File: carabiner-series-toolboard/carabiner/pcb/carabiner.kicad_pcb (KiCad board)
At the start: 2 copper layers, 32.1 x 35.5 mm, 25 parts, among them J1 MF-Vertical 43045-1612, J2 MF-Horizontal 43045-1621, J7 MF-Horizontal 43045-1600

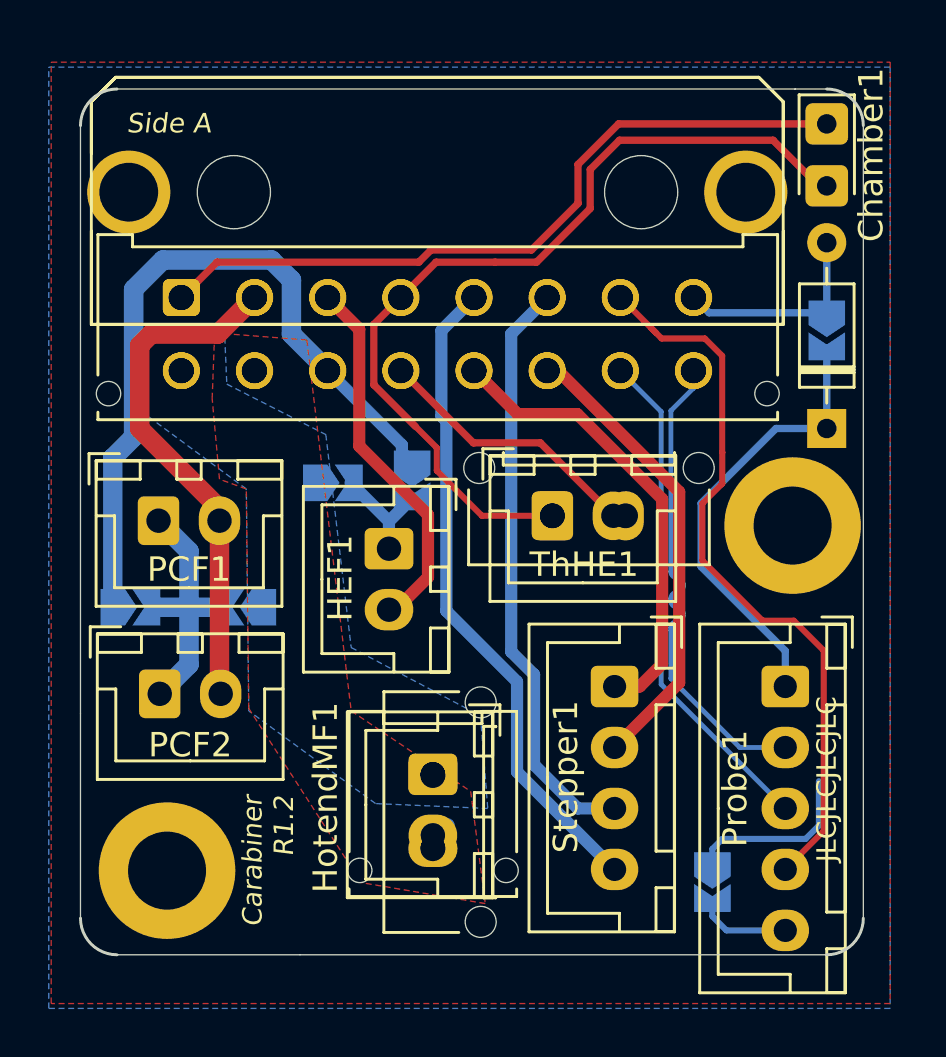
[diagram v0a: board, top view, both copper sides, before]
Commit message: Carabiner R1.2.1 - Fix all the things
- Fix disconnected A3 port (the 5th pin that duplicated A3 was disconnected)
- Match data lines closer - now within 0.04mm in length!
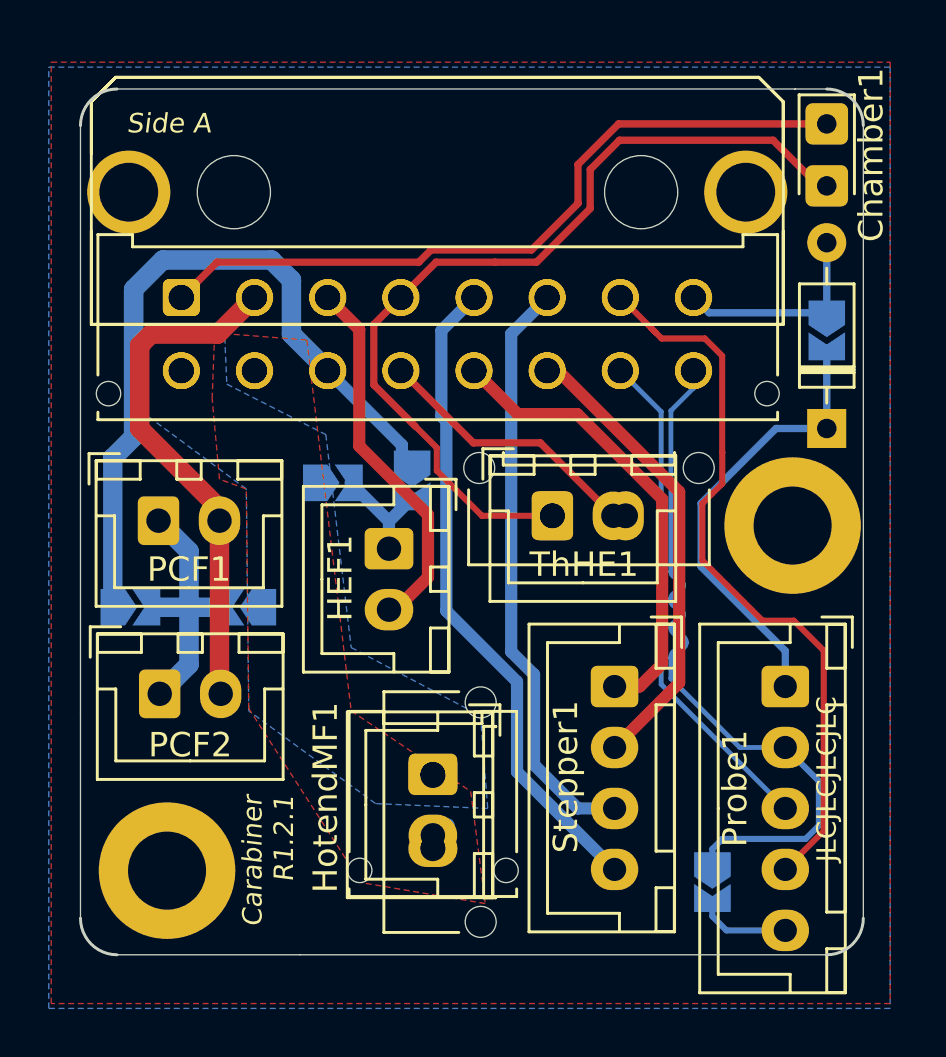
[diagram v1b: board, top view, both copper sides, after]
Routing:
- net A2+: track 27.5 -> 30.2 mm
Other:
- board text added: "Carabiner R1.2.1"
- board text removed: "Carabiner R1.2"
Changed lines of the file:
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@@
     (effects (font (size 0.7 0.7) (thickness 0.1)) (justify left mirror))
   )
-  (gr_text "Carabiner\nR1.2" (at 58.24 69.09 90) (layer "B.SilkS")
+  (gr_text "Carabiner\nR1.2.1" (at 58.24 69.09 90) (layer "B.SilkS")
     (effects (font (size 0.8 0.8) (thickness 0.15) italic) (justify right mirror))
   )
@@
     (effects (font (size 0.8 0.8) (thickness 0.15)))
   )
-  (gr_text "Carabiner\nR1.2" (at 58.2 62.97 90) (layer "F.SilkS")
+  (gr_text "Carabiner\nR1.2.1\n" (at 58.2 62.97 90) (layer "F.SilkS")
     (effects (font (size 0.8 0.8) (thickness 0.15) italic) (justify right))
   )
@@
   (segment (start 74.33 44.23) (end 73.915 43.815) (width 0.25) (layer "F.Cu") (net 10))
   (segment (start 76.1 44.23) (end 74.33 44.23) (width 0.25) (layer "F.Cu") (net 10))
-  (segment (start 75.63 46.27) (end 74.71 47.19) (width 0.2) (layer "B.Cu") (net 11))
+  (segment (start 74.71 54.89) (end 74.71 54.99) (width 0.2) (layer "B.Cu") (net 11))
+  (segment (start 75.039593 56.99) (end 75.01 56.99) (width 0.2) (layer "B.Cu") (net 11))
   (segment (start 76.82 64.75) (end 80.23 64.75) (width 0.25) (layer "B.Cu") (net 11))
   (segment (start 80.78 64.2) (end 80.78 62.38) (width 0.25) (layer "B.Cu") (net 11))
-  (segment (start 74.71 56.09) (end 74.71 56.19) (width 0.2) (layer "B.Cu") (net 11))
+  (segment (start 75.63 45.55) (end 75.63 46.27) (width 0.2) (layer "B.Cu") (net 11))
+  (segment (start 75.01 56.39) (end 75.039593 56.39) (width 0.2) (layer "B.Cu") (net 11))
+  (segment (start 77.536397 61) (end 79.4 61) (width 0.2) (layer "B.Cu") (net 11))
   (segment (start 74.71 47.19) (end 74.71 53.79) (width 0.2) (layer "B.Cu") (net 11))
+  (segment (start 75.21 55.49) (end 75.21 55.59) (width 0.2) (layer "B.Cu") (net 11))
   (segment (start 79.4 61) (end 79.4 60.63819) (width 0.25) (layer "B.Cu") (net 11))
-  (segment (start 74.71 54.89) (end 74.71 54.99) (width 0.2) (layer "B.Cu") (net 11))
   (segment (start 80.23 64.75) (end 80.78 64.2) (width 0.25) (layer "B.Cu") (net 11))
-  (segment (start 75.63 45.55) (end 75.63 46.27) (width 0.2) (layer "B.Cu") (net 11))
-  (segment (start 75.21 55.49) (end 75.21 55.59) (width 0.2) (layer "B.Cu") (net 11))
-  (segment (start 74.71 56.19) (end 74.71 58.173603) (width 0.2) (layer "B.Cu") (net 11))
+  (segment (start 74.71 57.29) (end 74.71 57.34) (width 0.2) (layer "B.Cu") (net 11))
+  (segment (start 75.63 46.27) (end 74.71 47.19) (width 0.2) (layer "B.Cu") (net 11))
   (segment (start 76.41 65.795) (end 76.41 65.16) (width 0.25) (layer "B.Cu") (net 11))
-  (segment (start 77.536397 61) (end 79.4 61) (width 0.2) (layer "B.Cu") (net 11))
+  (segment (start 75.21 54.29) (end 75.21 54.39) (width 0.2) (layer "B.Cu") (net 11))
+  (segment (start 80.78 62.38) (end 79.4 61) (width 0.25) (layer "B.Cu") (net 11))
   (segment (start 74.71 58.173603) (end 77.536397 61) (width 0.2) (layer "B.Cu") (net 11))
-  (segment (start 75.21 54.29) (end 75.21 54.39) (width 0.2) (layer "B.Cu") (net 11))
+  (segment (start 74.71 57.34) (end 74.71 58.173603) (width 0.2) (layer "B.Cu") (net 11))
   (segment (start 76.41 65.16) (end 76.82 64.75) (width 0.25) (layer "B.Cu") (net 11))
+  (arc (start 74.96 55.24) (mid 75.136777 55.313223) (end 75.21 55.49) (width 0.2) (layer "B.Cu") (net 11))
+  (arc (start 74.96 54.64) (mid 74.783223 54.713223) (end 74.71 54.89) (width 0.2) (layer "B.Cu") (net 11))
+  (arc (start 74.71 56.09) (mid 74.797868 56.302132) (end 75.01 56.39) (width 0.2) (layer "B.Cu") (net 11))
+  (arc (start 75.01 56.99) (mid 74.797868 57.077868) (end 74.71 57.29) (width 0.2) (layer "B.Cu") (net 11))
+  (arc (start 74.71 53.79) (mid 74.783223 53.966777) (end 74.96 54.04) (width 0.2) (layer "B.Cu") (net 11))
+  (arc (start 74.71 54.99) (mid 74.783223 55.166777) (end 74.96 55.24) (width 0.2) (layer "B.Cu") (net 11))
+  (arc (start 74.96 54.04) (mid 75.136777 54.113223) (end 75.21 54.29) (width 0.2) (layer "B.Cu") (net 11))
+  (arc (start 75.21 55.59) (mid 75.136777 55.766777) (end 74.96 55.84) (width 0.2) (layer "B.Cu") (net 11))
   (arc (start 75.21 54.39) (mid 75.136777 54.566777) (end 74.96 54.64) (width 0.2) (layer "B.Cu") (net 11))
-  (arc (start 75.21 55.59) (mid 75.136777 55.766777) (end 74.96 55.84) (width 0.2) (layer "B.Cu") (net 11))
-  (arc (start 74.71 53.79) (mid 74.783223 53.966777) (end 74.96 54.04) (width 0.2) (layer "B.Cu") (net 11))
+  (arc (start 75.039593 56.39) (mid 75.251725 56.477868) (end 75.339593 56.69) (width 0.2) (layer "B.Cu") (net 11))
+  (arc (start 75.339593 56.69) (mid 75.251725 56.902132) (end 75.039593 56.99) (width 0.2) (layer "B.Cu") (net 11))
   (arc (start 74.96 55.84) (mid 74.783223 55.913223) (end 74.71 56.09) (width 0.2) (layer "B.Cu") (net 11))
-  (arc (start 74.96 55.24) (mid 75.136777 55.313223) (end 75.21 55.49) (width 0.2) (layer "B.Cu") (net 11))
-  (arc (start 74.96 54.04) (mid 75.136777 54.113223) (end 75.21 54.29) (width 0.2) (layer "B.Cu") (net 11))
-  (arc (start 74.96 54.64) (mid 74.783223 54.713223) (end 74.71 54.89) (width 0.2) (layer "B.Cu") (net 11))
-  (arc (start 74.71 54.99) (mid 74.783223 55.166777) (end 74.96 55.24) (width 0.2) (layer "B.Cu") (net 11))
   (segment (start 72.63 45.55) (end 74.31 47.23) (width 0.2) (layer "B.Cu") (net 12))
   (segment (start 74.31 47.23) (end 74.31 58.41) (width 0.2) (layer "B.Cu") (net 12))
